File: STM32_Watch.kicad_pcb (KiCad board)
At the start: 2 copper layers, 40 x 45 mm, 44 parts, among them SW1 SW_Push, SW2 SW_Push, U1 STM32L031K6Ux, U2 LSM6DS3, X1 32.768k

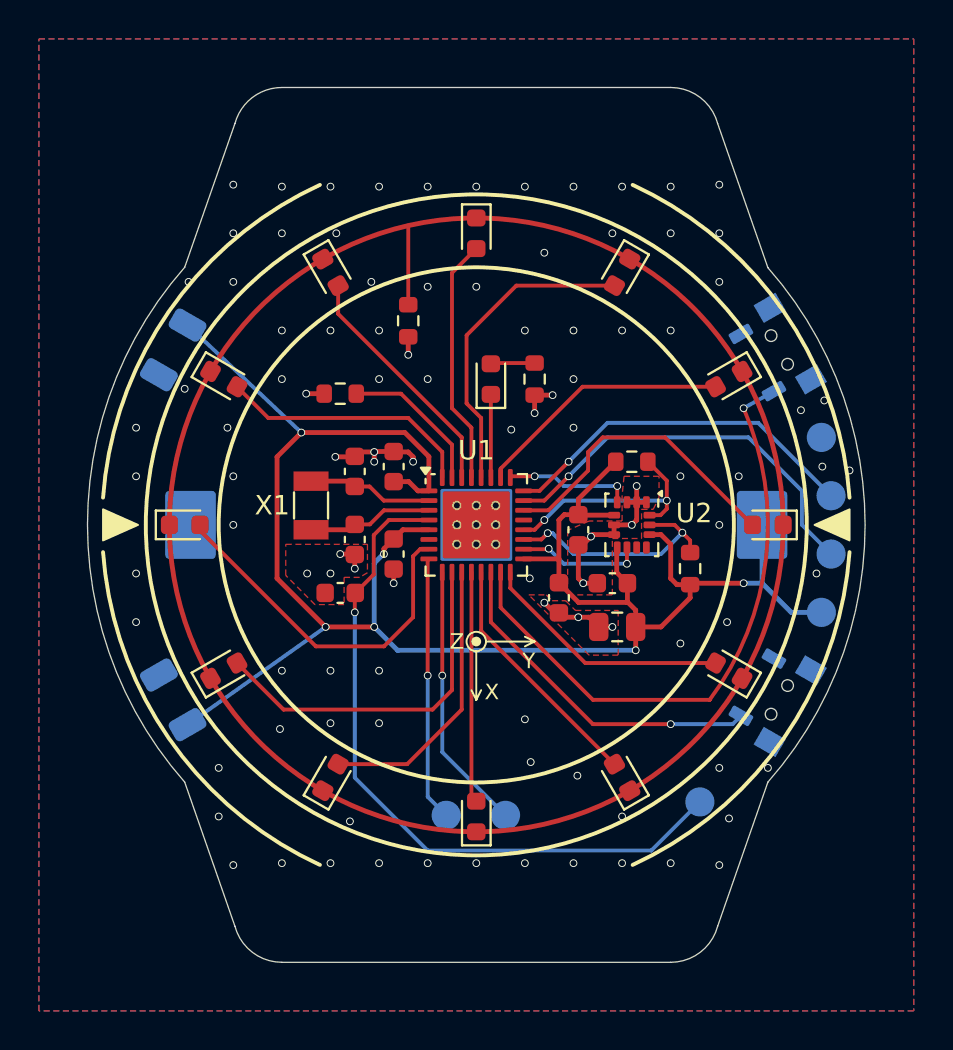
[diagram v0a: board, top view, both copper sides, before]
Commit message: Improved routing
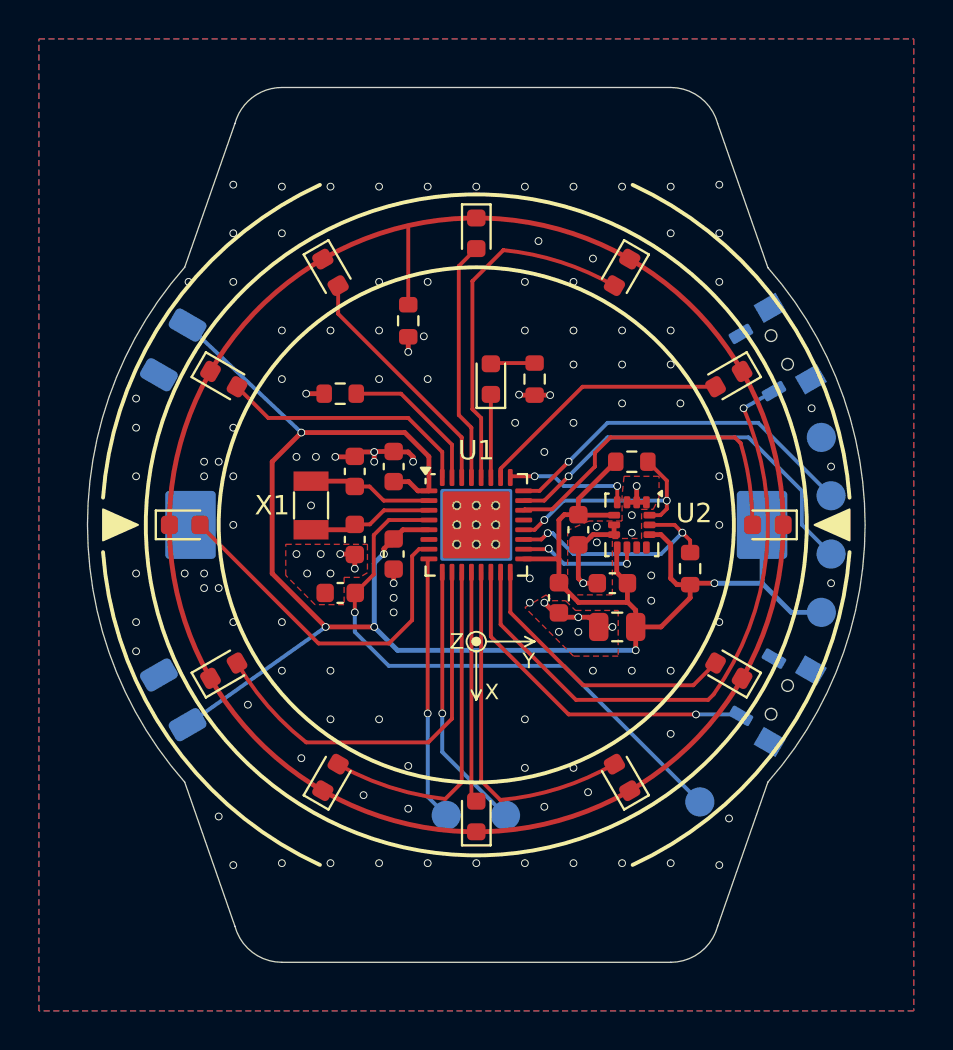
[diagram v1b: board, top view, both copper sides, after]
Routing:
- net /NRST: track 36.4 -> 29.9 mm
- net LED_1: track 16.3 -> 12.5 mm
- net LED_8: track 18.5 -> 15.5 mm
- net GND: track 24.5 -> 22.0 mm, vias 103 -> 133
- net LED_7: track 14.6 -> 12.0 mm
- net LED_3: track 15.8 -> 13.3 mm
- net LED_4: track 13.0 -> 14.6 mm
- net SW1: track 14.5 -> 15.4 mm
- net LED_5: track 12.7 -> 12.1 mm

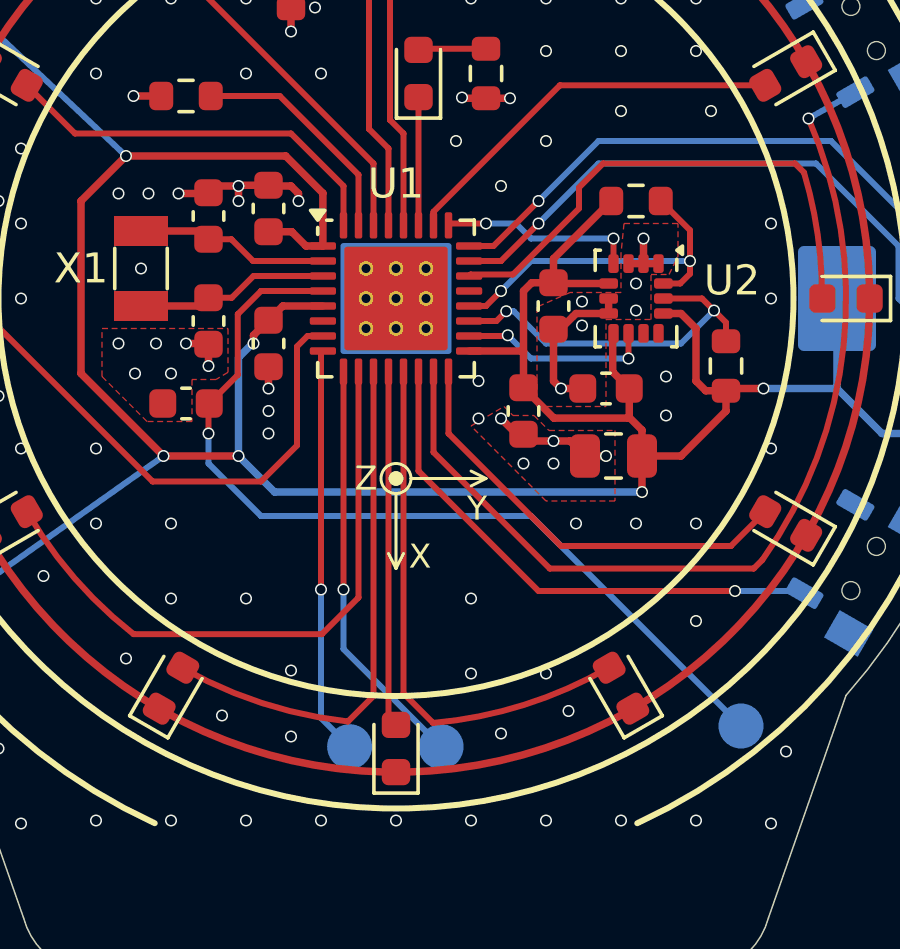
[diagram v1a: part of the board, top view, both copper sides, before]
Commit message: Added GND TP & BOM file
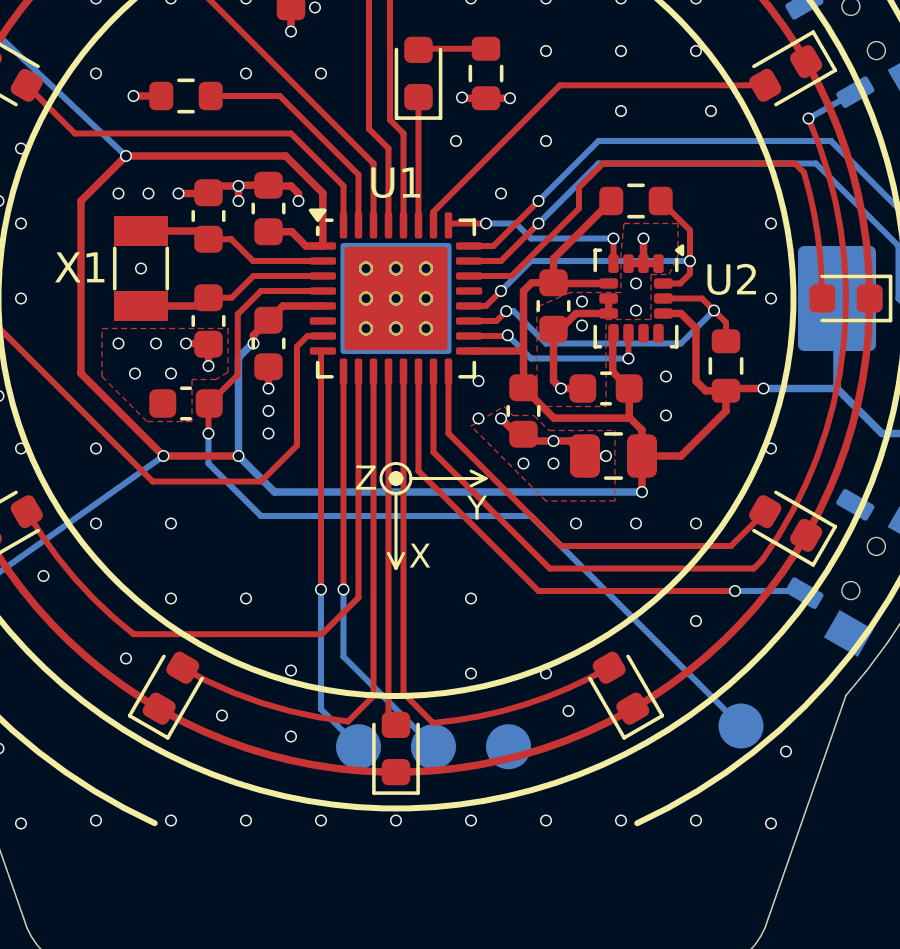
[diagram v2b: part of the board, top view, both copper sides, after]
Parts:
- added TP2: TestPoint_Small, TestPoint:TestPoint_Pad_D1.5mm, B.Cu at (103.8, 114.9)
- moved TP7 0.30 mm to (98.8, 114.9)
- moved TP8 0.25 mm to (101.2, 114.9)
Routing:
- net GND: vias 133 -> 132
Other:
- board text added: "GN"
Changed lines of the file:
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@@
 			)
 		)
-		(property "LCSC" "C967633"
+		(property "LCSC" "C94048"
 			(at 0 0 270)
 			(unlocked yes)
@@
 		(layer "F.Cu")
 		(at 100 81)
-		(descr "Mounting Hole 2.2mm, no annular, M2")
-		(tags "mounting hole 2.2mm no annular m2")
 		(property "Reference" "H1"
 			(at 0 -3.2 0)
@@
 		(layer "F.Cu")
 		(at 100 119)
-		(descr "Mounting Hole 2.2mm, no annular, M2")
-		(tags "mounting hole 2.2mm no annular m2")
 		(property "Reference" "H2"
 			(at 0 -3.2 0)
@@
 			)
 		)
-		(property "LCSC" "C15850"
+		(property "LCSC" "C32635"
 			(at 0 0 180)
 			(unlocked yes)
@@
 	(footprint "TestPoint:TestPoint_Pad_D1.5mm"
 		(layer "B.Cu")
+		(at 103.75 114.939826 180)
+		(descr "SMD pad as test Point, diameter 1.5mm")
+		(tags "test point SMD pad")
+		(property "Reference" "TP2"
+			(at 0 1.648 0)
+			(layer "B.SilkS")
+			(hide yes)
+			(effects
+				(font
+					(size 1 1)
+					(thickness 0.15)
+				)
+				(justify mirror)
+			)
+		)
+		(property "Value" "TestPoint_Small"
+			(at 0 -1.75 0)
+			(layer "B.Fab")
+			(effects
+				(font
+					(size 1 1)
+					(thickness 0.15)
+				)
+				(justify mirror)
+			)
+		)
+		(property "Datasheet" ""
+			(at 0 0 0)
+			(unlocked yes)
+			(layer "B.Fab")
+			(hide yes)
+			(effects
+				(font
+					(size 1.27 1.27)
+					(thickness 0.15)
+				)
+				(justify mirror)
+			)
+		)
+		(property "Description" "test point"
+			(at 0 0 0)
+			(unlocked yes)
+			(layer "B.Fab")
+			(hide yes)
+			(effects
+				(font
+					(size 1.27 1.27)
+					(thickness 0.15)
+				)
+				(justify mirror)
+			)
+		)
+		(property ki_fp_filters "Pin* Test*")
+		(sheetname "/")
+		(sheetfile "STM32_Watch.kicad_sch")
+		(attr exclude_from_pos_files)
+		(fp_circle
+			(center 0 0)
+			(end 0 -0.95)
+			(stroke
+				(width 0.12)
+				(type solid)
+			)
+			(fill no)
+			(layer "B.SilkS")
+		)
+		(fp_circle
+			(center 0 0)
+			(end 1.25 0)
+			(stroke
+				(width 0.05)
+				(type solid)
+			)
+			(fill no)
+			(layer "B.CrtYd")
+		)
+		(fp_text user "${REFERENCE}"
+			(at 0 1.65 0)
+			(layer "B.Fab")
+			(effects
+				(font
+					(size 1 1)
+					(thickness 0.15)
+				)
+				(justify mirror)
+			)
+		)
+		(pad "1" smd circle
+			(at 0 0 180)
+			(size 1.5 1.5)
+			(layers "B.Cu" "B.Mask")
+			(net 2 "GND")
+			(pinfunction "1")
+			(pintype "passive")
+		)
+		(embedded_fonts no)
+	)
+	(footprint "TestPoint:TestPoint_Pad_D1.5mm"
+		(layer "B.Cu")
 		(at 117.75 104.5 -90)
 		(descr "SMD pad as test Point, diameter 1.5mm")
@@
 	(footprint "TestPoint:TestPoint_Pad_D1.5mm"
 		(layer "B.Cu")
-		(at 101.503735 114.939826 -90)
+		(at 101.25 114.939826 -90)
 		(descr "SMD pad as test Point, diameter 1.5mm")
 		(tags "test point SMD pad")
@@
 	(footprint "TestPoint:TestPoint_Pad_D1.5mm"
 		(layer "B.Cu")
-		(at 98.453735 114.939826 -90)
+		(at 98.75 114.939826 -90)
 		(descr "SMD pad as test Point, diameter 1.5mm")
 		(tags "test point SMD pad")
@@
 		)
 	)
+	(gr_text "GN"
+		(at 103.75 113 0)
+		(layer "B.SilkS" knockout)
+		(effects
+			(font
+				(size 1 1)
+				(thickness 0.2)
+				(bold yes)
+			)
+			(justify mirror)
+		)
+	)
 	(gr_text "3V3"
 		(at 116.5 105.6 0)
@@
 	)
 	(gr_text "TX"
-		(at 99.4 113.6 0)
+		(at 98.75 113 0)
 		(layer "B.SilkS" knockout)
 		(effects
@@
 				(bold yes)
 			)
-			(justify left bottom mirror)
+			(justify mirror)
 		)
 	)
 	(gr_text "RX"
-		(at 102.7 113.6 0)
+		(at 101.25 113 0)
 		(layer "B.SilkS" knockout)
 		(effects
@@
 				(bold yes)
 			)
-			(justify left bottom mirror)
+			(justify mirror)
 		)
 	)
@@
 	)
 	(via
-		(at 103.5 114.5)
-		(size 0.4)
-		(drill 0.3)
-		(layers "F.Cu" "B.Cu")
-		(free yes)
-		(net 2)
-	)
-	(via
 		(at 91.25 93.25)
 		(size 0.4)
@@
 	)
 	(via
+		(at 103.5 96.5)
+		(size 0.4)
+		(drill 0.3)
+		(layers "F.Cu" "B.Cu")
+		(free yes)
+		(net 2)
+	)
+	(via
 		(at 110.5 93.75)
 		(size 0.4)
@@
 	)
 	(via
-		(at 103.5 96.25)
-		(size 0.4)
-		(drill 0.3)
-		(layers "F.Cu" "B.Cu")
-		(free yes)
-		(net 2)
-	)
-	(via
 		(at 108 100.4)
 		(size 0.4)
@@
 	)
 	(segment
-		(start 106.9 95.5)
-		(end 113.3 95.5)
-		(width 0.2)
-		(layer "F.Cu")
-		(net 9)
-	)
-	(segment
 		(start 113.3 95.5)
 		(end 113.6 95.8)
@@
 	)
 	(segment
-		(start 103.9 99.2)
-		(end 106.1 97)
+		(start 106.1 96.3)
+		(end 106.9 95.5)
 		(width 0.2)
 		(layer "F.Cu")
@@
 	)
 	(segment
-		(start 106.1 97)
-		(end 106.1 96.3)
+		(start 102.4375 99.25)
+		(end 103.85 99.25)
 		(width 0.2)
 		(layer "F.Cu")
@@
 	)
 	(segment
-		(start 102.4375 99.25)
-		(end 102.4875 99.2)
+		(start 106.1 97)
+		(end 106.1 96.3)
 		(width 0.2)
 		(layer "F.Cu")
@@
 	)
 	(segment
-		(start 102.4875 99.2)
-		(end 103.9 99.2)
+		(start 103.85 99.25)
+		(end 106.1 97)
 		(width 0.2)
 		(layer "F.Cu")
@@
 	)
 	(segment
-		(start 106.1 96.3)
-		(end 106.9 95.5)
+		(start 106.9 95.5)
+		(end 113.3 95.5)
 		(width 0.2)
 		(layer "F.Cu")
@@
 	(segment
 		(start 97.5 109.7)
-		(end 97.5 113.986091)
+		(end 97.5 113.689826)
 		(width 0.2)
 		(layer "B.Cu")
@@
 	)
 	(segment
-		(start 97.5 113.986091)
-		(end 98.453735 114.939826)
+		(start 97.5 113.689826)
+		(end 98.75 114.939826)
 		(width 0.2)
 		(layer "B.Cu")
@@
 	)
 	(segment
-		(start 98.25 111.686091)
-		(end 101.503735 114.939826)
+		(start 98.25 111.939826)
+		(end 101.25 114.939826)
 		(width 0.2)
 		(layer "B.Cu")
@@
 	(segment
 		(start 98.25 109.7)
-		(end 98.25 111.686091)
+		(end 98.25 111.939826)
 		(width 0.2)
 		(layer "B.Cu")

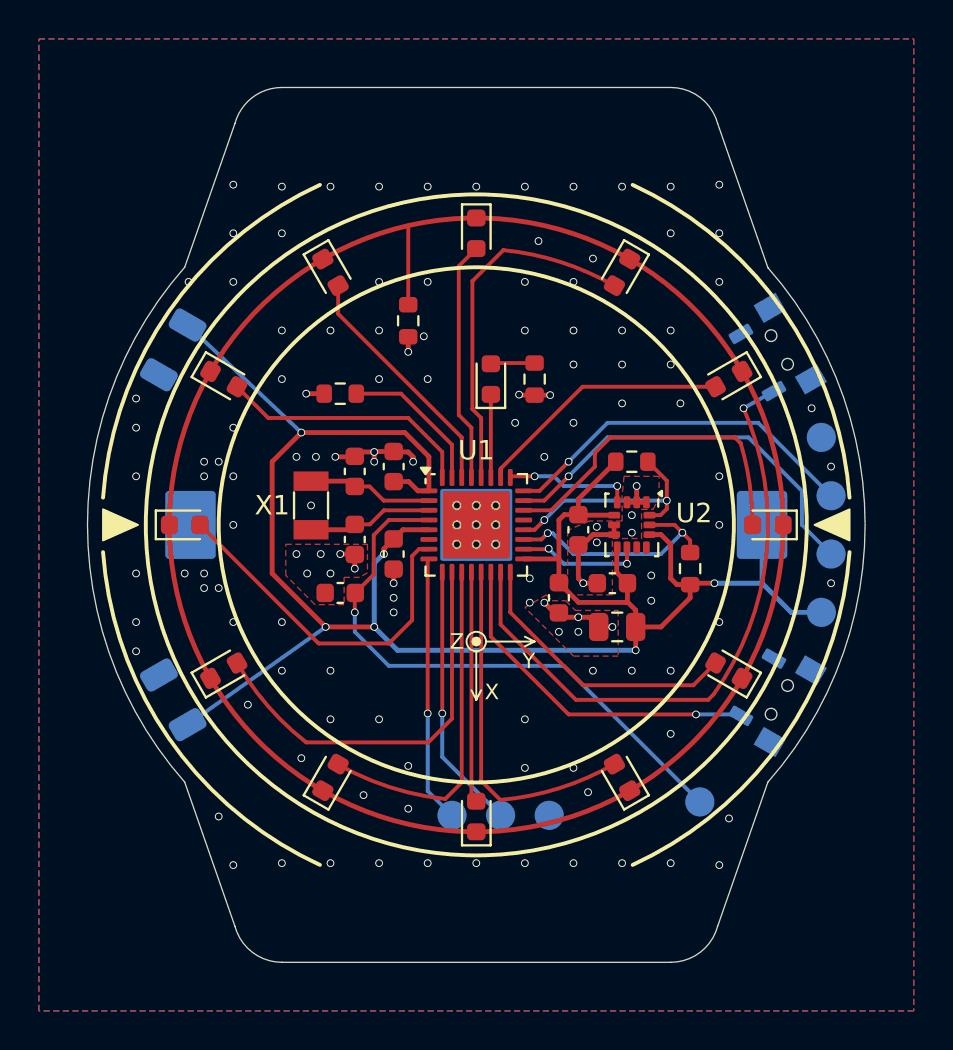
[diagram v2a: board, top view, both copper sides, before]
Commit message: Vias dim 0.4 -> 0.5
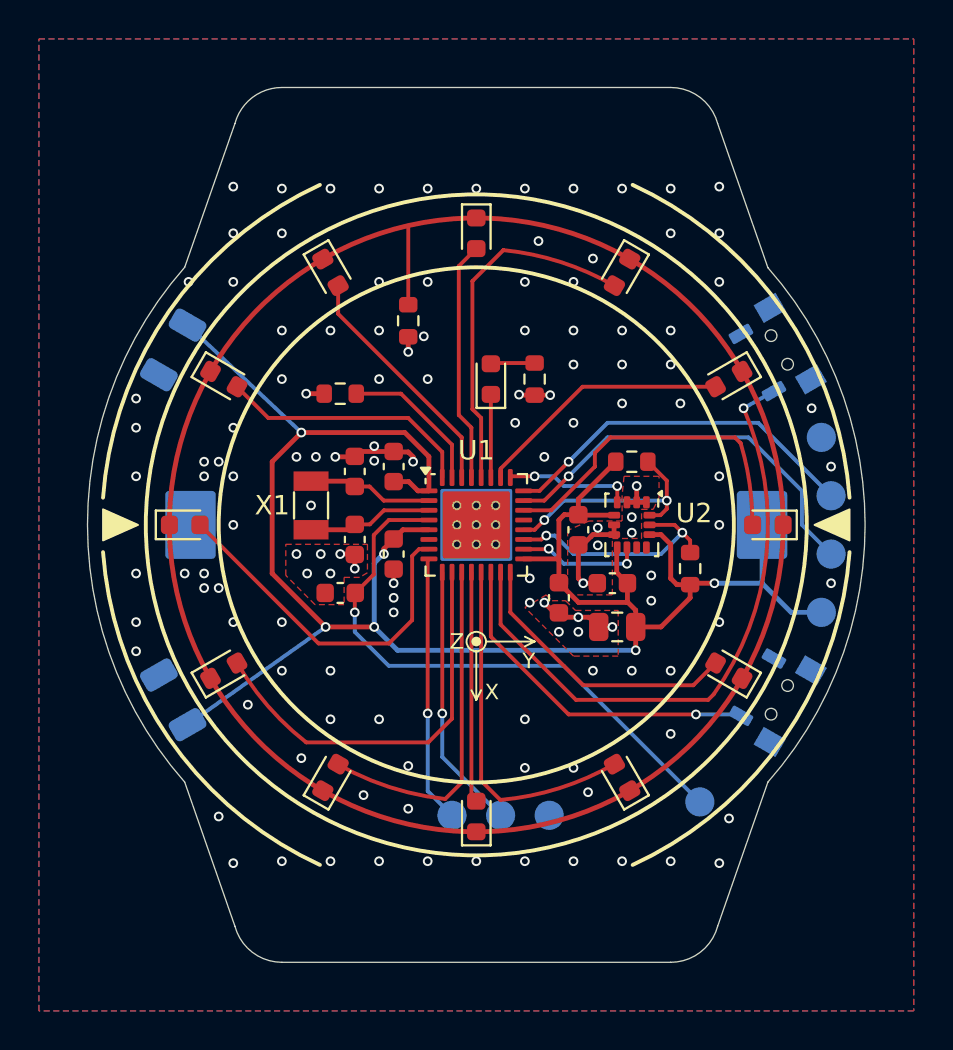
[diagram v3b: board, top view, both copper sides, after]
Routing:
- net GND: track 22.0 -> 21.5 mm
